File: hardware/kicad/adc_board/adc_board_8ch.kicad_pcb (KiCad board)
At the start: 2 copper layers, 88 x 66 mm, 10 parts, among them J1 ELECTRODES, J2 SPI_HOST, J3 PWR_CTRL, U1 ADS131M08

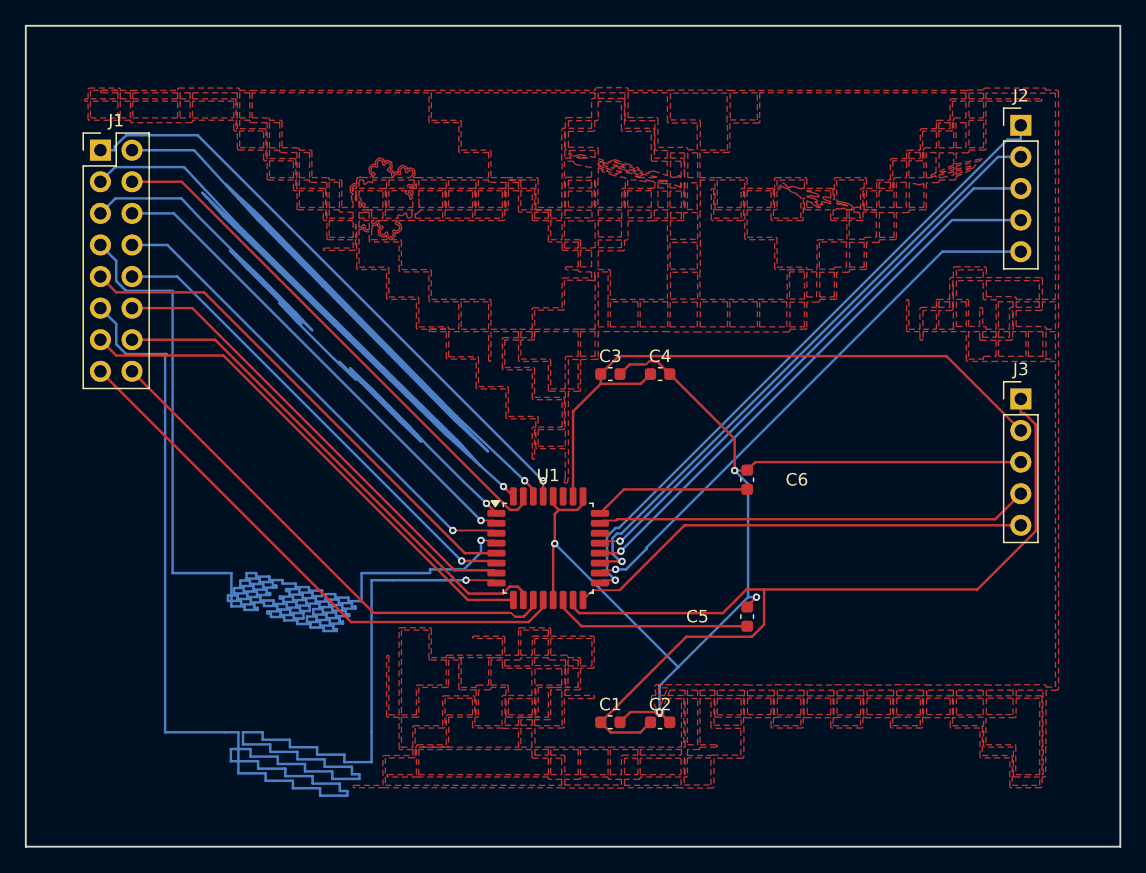
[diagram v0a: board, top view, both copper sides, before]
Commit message: feat(kicad): add dense dual-layer copper weave
Co-authored-by: Copilot <223556219+Copilot@users.noreply.github.com>
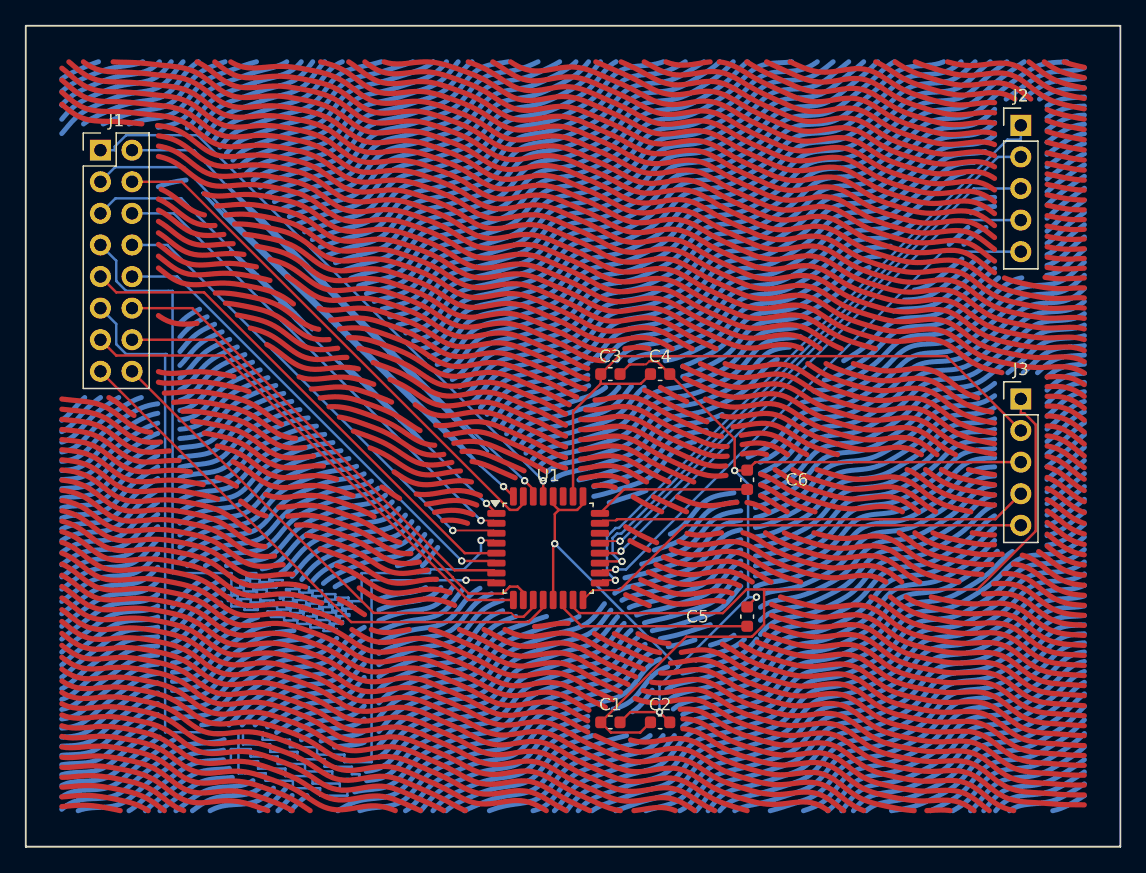
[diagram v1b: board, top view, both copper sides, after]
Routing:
- removed copper zone on F.Cu, net GND

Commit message: feat(kicad): hide more adc traces in weave
Co-authored-by: Copilot <223556219+Copilot@users.noreply.github.com>
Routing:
- net AIN0P: track 49.0 -> 168.5 mm
- net AIN2N: track 39.6 -> 154.4 mm
- net AIN3N: track 38.9 -> 145.5 mm
- net AIN4N: track 38.8 -> 79.3 mm

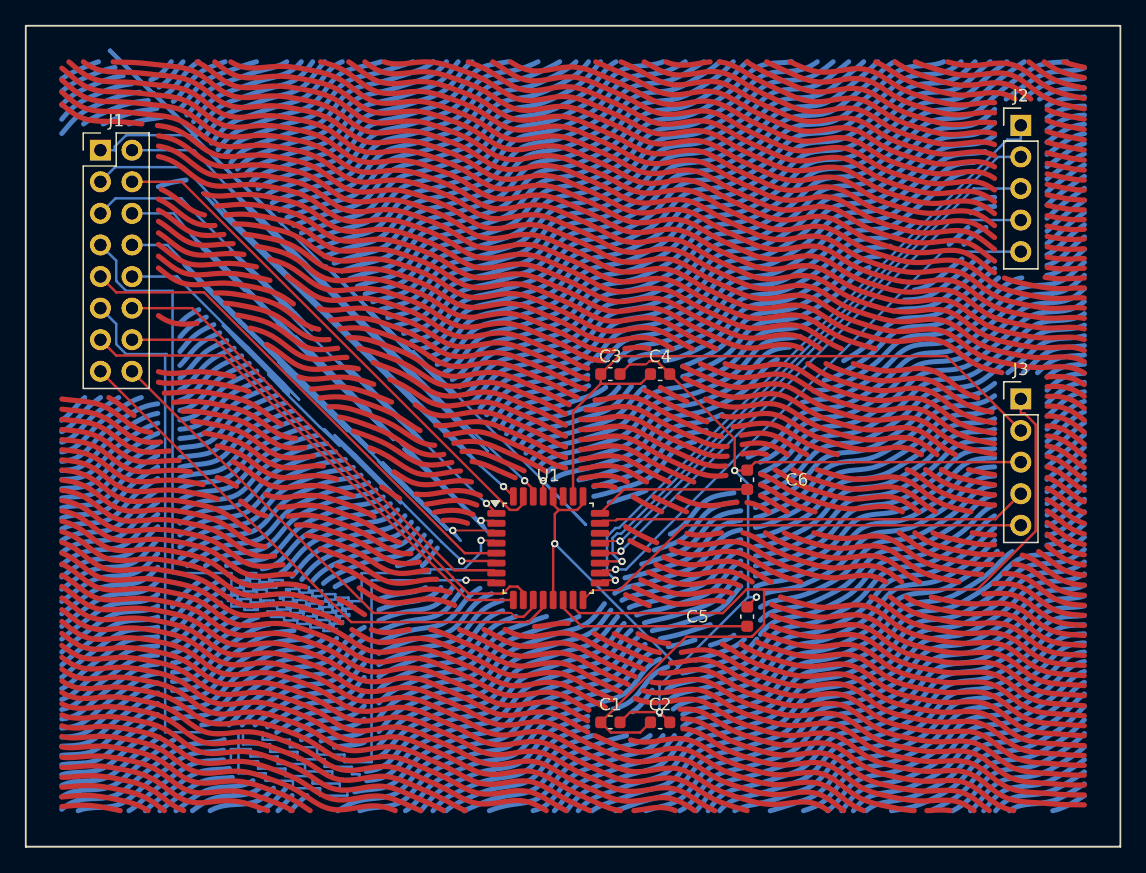
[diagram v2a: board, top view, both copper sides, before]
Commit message: feat(kicad): hide more adc traces on top layer
Co-authored-by: Copilot <223556219+Copilot@users.noreply.github.com>
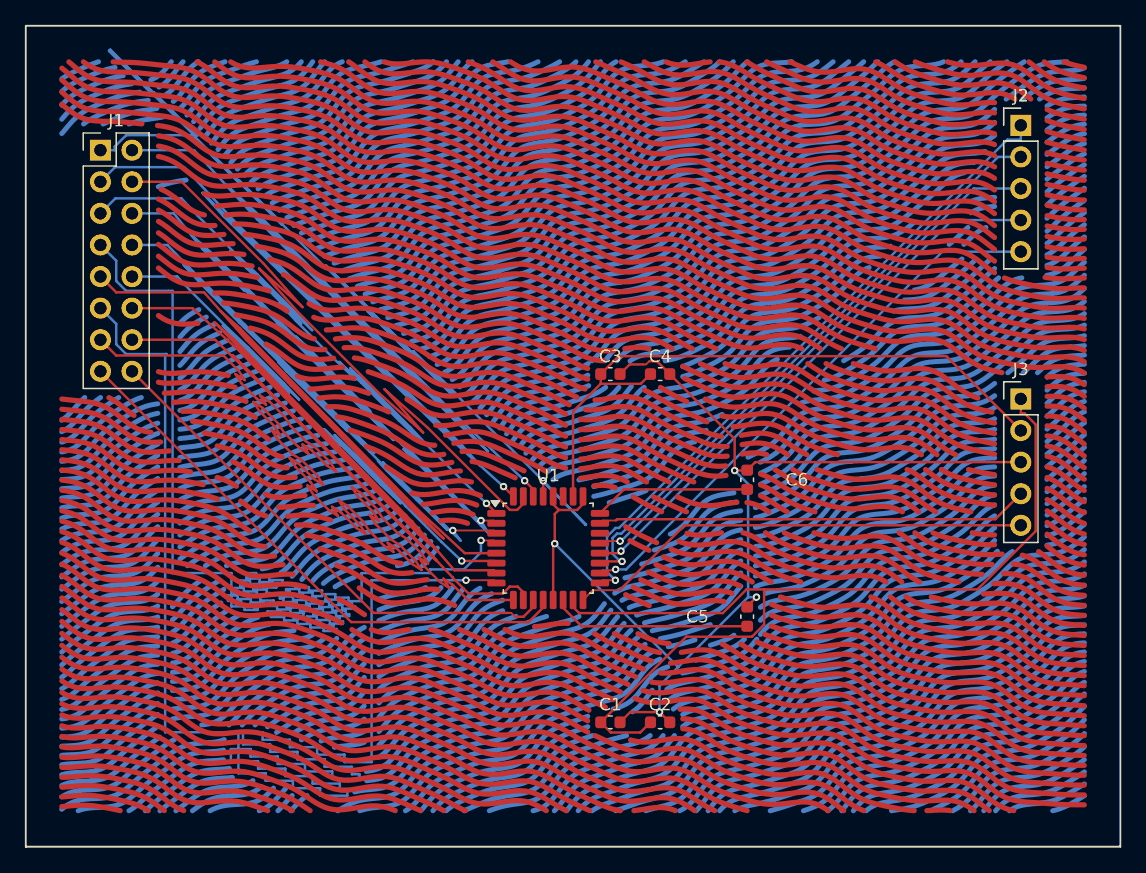
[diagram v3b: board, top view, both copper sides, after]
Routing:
- net AIN6P: track 41.9 -> 108.9 mm
- net AIN5N: track 38.1 -> 89.5 mm
- net AIN4P: track 41.0 -> 92.2 mm
- net AIN6N: track 41.0 -> 87.6 mm
- net AIN1N: track 43.2 -> 61.9 mm
